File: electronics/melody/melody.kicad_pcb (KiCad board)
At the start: 2 copper layers, 8 parts, among them J1 USB_B, J2 Raspberry_Pi_4, J3 Conn_01x04_Pin, J4 Conn_01x01_Pin, J5 Conn_01x16_Pin, J6 Conn_01x16_Pin, U1 74154, U2 74154

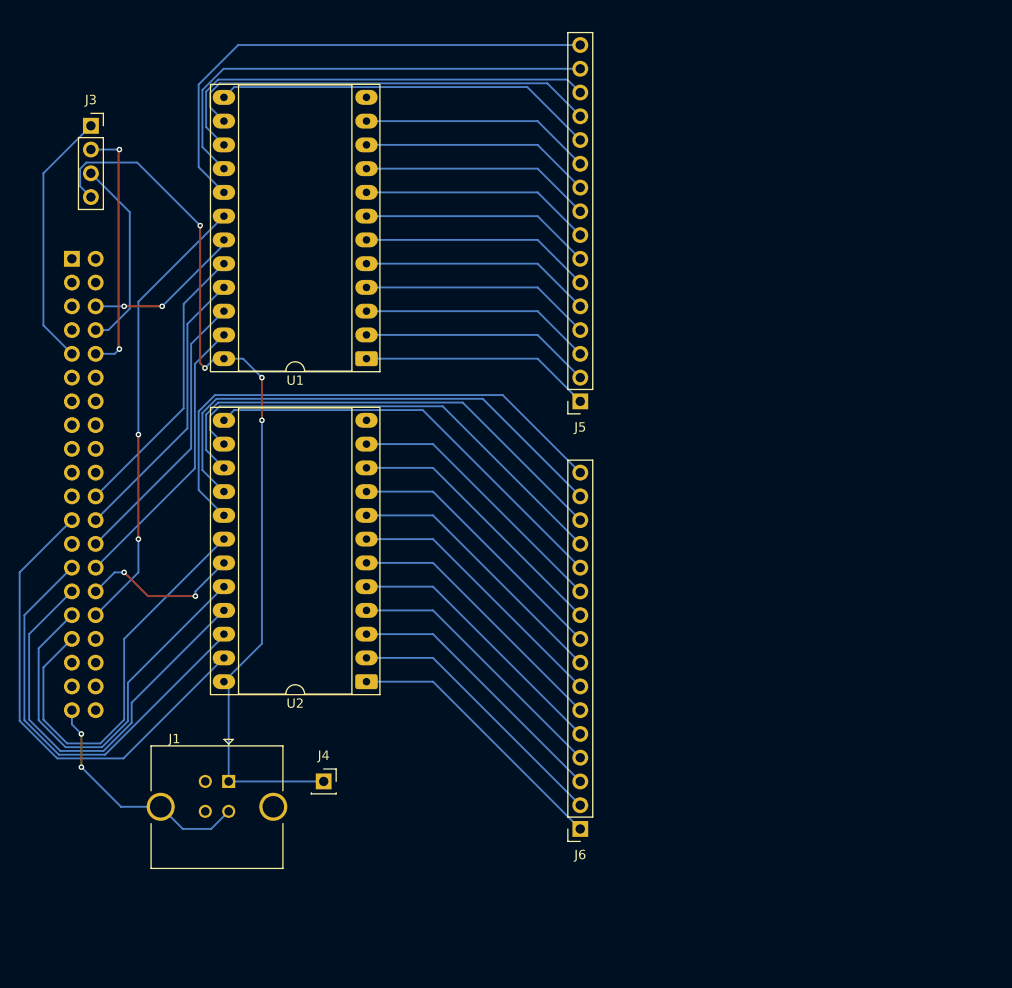
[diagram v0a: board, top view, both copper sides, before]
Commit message: change IC 74->40 + shared power supply for processors + PCB
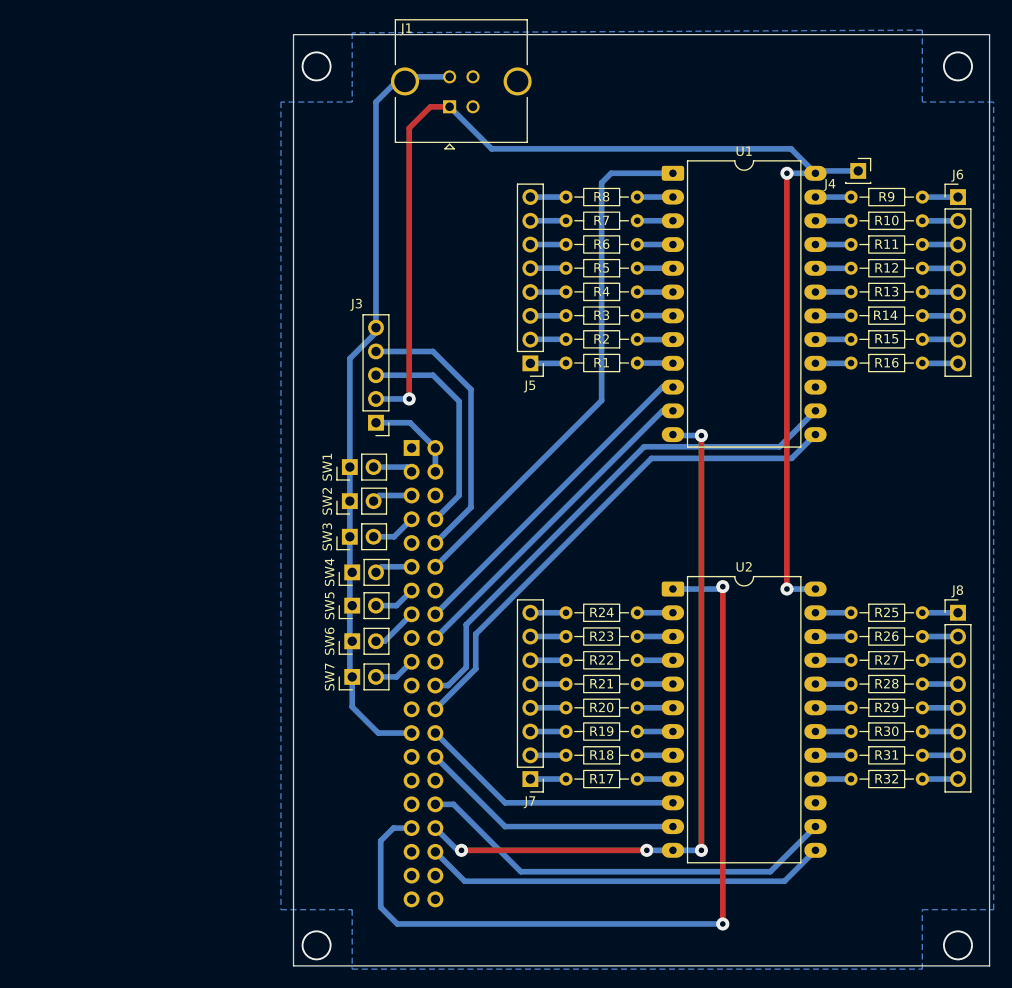
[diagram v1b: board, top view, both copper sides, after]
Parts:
- added J7: Conn_01x08_Pin, Connector_PinHeader_2.54mm:PinHeader_1x08_P2.54mm_Vertical, F.Cu at (135.9, 125.7)
- added J8: Conn_01x08_Pin, Connector_PinHeader_2.54mm:PinHeader_1x08_P2.54mm_Vertical, F.Cu at (181.6, 108.0)
- added R1: 270R, Resistor_THT:R_Axial_DIN0204_L3.6mm_D1.6mm_P7.62mm_Horizontal, F.Cu at (147.3, 81.2)
- added R10: 270R, Resistor_THT:R_Axial_DIN0204_L3.6mm_D1.6mm_P7.62mm_Horizontal, F.Cu at (170.2, 66.0)
- added R11: 270R, Resistor_THT:R_Axial_DIN0204_L3.6mm_D1.6mm_P7.62mm_Horizontal, F.Cu at (170.2, 68.6)
- added R12: 270R, Resistor_THT:R_Axial_DIN0204_L3.6mm_D1.6mm_P7.62mm_Horizontal, F.Cu at (170.2, 71.1)
- added R13: 270R, Resistor_THT:R_Axial_DIN0204_L3.6mm_D1.6mm_P7.62mm_Horizontal, F.Cu at (170.2, 73.6)
- added R14: 270R, Resistor_THT:R_Axial_DIN0204_L3.6mm_D1.6mm_P7.62mm_Horizontal, F.Cu at (170.2, 76.2)
- added R15: 270R, Resistor_THT:R_Axial_DIN0204_L3.6mm_D1.6mm_P7.62mm_Horizontal, F.Cu at (170.2, 78.7)
- added R16: 270R, Resistor_THT:R_Axial_DIN0204_L3.6mm_D1.6mm_P7.62mm_Horizontal, F.Cu at (170.2, 81.3)
- added R17: 330R, Resistor_THT:R_Axial_DIN0204_L3.6mm_D1.6mm_P7.62mm_Horizontal, F.Cu at (147.3, 125.7)
- added R18: 330R, Resistor_THT:R_Axial_DIN0204_L3.6mm_D1.6mm_P7.62mm_Horizontal, F.Cu at (147.3, 123.2)
- added R19: 330R, Resistor_THT:R_Axial_DIN0204_L3.6mm_D1.6mm_P7.62mm_Horizontal, F.Cu at (147.3, 120.7)
- added R2: 270R, Resistor_THT:R_Axial_DIN0204_L3.6mm_D1.6mm_P7.62mm_Horizontal, F.Cu at (147.3, 78.7)
- added R20: 330R, Resistor_THT:R_Axial_DIN0204_L3.6mm_D1.6mm_P7.62mm_Horizontal, F.Cu at (147.3, 118.1)
- added R21: 330R, Resistor_THT:R_Axial_DIN0204_L3.6mm_D1.6mm_P7.62mm_Horizontal, F.Cu at (147.3, 115.6)
- added R22: 330R, Resistor_THT:R_Axial_DIN0204_L3.6mm_D1.6mm_P7.62mm_Horizontal, F.Cu at (147.3, 113.0)
- added R23: 330R, Resistor_THT:R_Axial_DIN0204_L3.6mm_D1.6mm_P7.62mm_Horizontal, F.Cu at (147.3, 110.5)
- added R24: 330R, Resistor_THT:R_Axial_DIN0204_L3.6mm_D1.6mm_P7.62mm_Horizontal, F.Cu at (147.3, 108.0)
- added R25: 330R, Resistor_THT:R_Axial_DIN0204_L3.6mm_D1.6mm_P7.62mm_Horizontal, F.Cu at (170.2, 108.0)
- added R26: 330R, Resistor_THT:R_Axial_DIN0204_L3.6mm_D1.6mm_P7.62mm_Horizontal, F.Cu at (170.2, 110.5)
- added R27: 330R, Resistor_THT:R_Axial_DIN0204_L3.6mm_D1.6mm_P7.62mm_Horizontal, F.Cu at (170.2, 113.0)
- added R28: 330R, Resistor_THT:R_Axial_DIN0204_L3.6mm_D1.6mm_P7.62mm_Horizontal, F.Cu at (170.2, 115.6)
- added R29: 330R, Resistor_THT:R_Axial_DIN0204_L3.6mm_D1.6mm_P7.62mm_Horizontal, F.Cu at (170.2, 118.1)
- added R3: 270R, Resistor_THT:R_Axial_DIN0204_L3.6mm_D1.6mm_P7.62mm_Horizontal, F.Cu at (147.3, 76.2)
- added R30: 330R, Resistor_THT:R_Axial_DIN0204_L3.6mm_D1.6mm_P7.62mm_Horizontal, F.Cu at (170.2, 120.7)
- added R31: 330R, Resistor_THT:R_Axial_DIN0204_L3.6mm_D1.6mm_P7.62mm_Horizontal, F.Cu at (170.2, 123.2)
- added R32: 330R, Resistor_THT:R_Axial_DIN0204_L3.6mm_D1.6mm_P7.62mm_Horizontal, F.Cu at (170.2, 125.7)
- added R4: 270R, Resistor_THT:R_Axial_DIN0204_L3.6mm_D1.6mm_P7.62mm_Horizontal, F.Cu at (147.3, 73.6)
- added R5: 270R, Resistor_THT:R_Axial_DIN0204_L3.6mm_D1.6mm_P7.62mm_Horizontal, F.Cu at (147.3, 71.1)
- added R6: 270R, Resistor_THT:R_Axial_DIN0204_L3.6mm_D1.6mm_P7.62mm_Horizontal, F.Cu at (147.3, 68.6)
- added R7: 270R, Resistor_THT:R_Axial_DIN0204_L3.6mm_D1.6mm_P7.62mm_Horizontal, F.Cu at (147.3, 66.0)
- added R8: 270R, Resistor_THT:R_Axial_DIN0204_L3.6mm_D1.6mm_P7.62mm_Horizontal, F.Cu at (147.3, 63.5)
- added R9: 270R, Resistor_THT:R_Axial_DIN0204_L3.6mm_D1.6mm_P7.62mm_Horizontal, F.Cu at (170.2, 63.5)
- added SW1: SW_Push, Connector_PinHeader_2.54mm:PinHeader_1x02_P2.54mm_Vertical, F.Cu at (116.6, 92.4)
- added SW2: SW_Push, Connector_PinHeader_2.54mm:PinHeader_1x02_P2.54mm_Vertical, F.Cu at (116.6, 96.0)
- added SW3: SW_Push, Connector_PinHeader_2.54mm:PinHeader_1x02_P2.54mm_Vertical, F.Cu at (116.6, 99.8)
- added SW4: SW_Push, Connector_PinHeader_2.54mm:PinHeader_1x02_P2.54mm_Vertical, F.Cu at (116.8, 103.6)
- added SW5: SW_Push, Connector_PinHeader_2.54mm:PinHeader_1x02_P2.54mm_Vertical, F.Cu at (116.8, 107.2)
- added SW6: SW_Push, Connector_PinHeader_2.54mm:PinHeader_1x02_P2.54mm_Vertical, F.Cu at (116.8, 111.0)
- added SW7: SW_Push, Connector_PinHeader_2.54mm:PinHeader_1x02_P2.54mm_Vertical, F.Cu at (116.8, 114.8)
- J3: value Conn_01x04_Pin -> Conn_01x05_Pin; footprint Connector_PinSocket_2.54mm:PinSocket_1x04_P2.54mm_Vertical -> Connector_PinHeader_2.54mm:PinHeader_1x05_P2.54mm_Vertical
- J5, J6: value Conn_01x16_Pin -> Conn_01x08_Pin; footprint Connector_PinSocket_2.54mm:PinSocket_1x16_P2.54mm_Vertical -> Connector_PinHeader_2.54mm:PinHeader_1x08_P2.54mm_Vertical
- U1, U2: value 74154 -> CD4067; footprint Package_DIP:DIP-24_W15.24mm_Socket_LongPads -> Package_DIP:DIP-24_W15.24mm_LongPads
- moved J4 86.8 mm to (170.9, 60.7)
- moved J6 78.7 mm to (181.6, 63.5), turned to 0 degrees
- moved J1 75.9 mm to (127.3, 53.8), turned to 180 degrees
- moved J3 44.0 mm to (119.4, 87.6), turned to 180 degrees
- moved J2 41.6 mm to (123.2, 90.3)
- moved U1 38.3 mm to (151.1, 61.0), turned to 0 degrees
- moved U2 34.2 mm to (151.1, 105.4), turned to 0 degrees
- moved J5 6.71 mm to (135.9, 81.3)
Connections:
- J2 pad 11: unconnected-(J2-GPIO17/SPI1_~{CE1}-Pad11) -> /BT_4
- J2 pad 12: unconnected-(J2-GPIO18/SPI1_~{CE0}/PCM_CLK/PWM0-Pad12) -> /PWM_GREEN
- J2 pad 13: unconnected-(J2-GPIO27/SDIO_DAT3-Pad13) -> /BT_5
- J2 pad 15: unconnected-(J2-GPIO22/SDIO_CLK-Pad15) -> /BT_6
- J2 pad 16: unconnected-(J2-GPIO23/SDIO_CMD-Pad16) -> /G0
- J2 pad 18: unconnected-(J2-GPIO24/SDIO_DAT0-Pad18) -> /G1
- J2 pad 19: unconnected-(J2-MOSI_SPI0/GPIO10-Pad19) -> /BT_7
- J2 pad 2: unconnected-(J2-5V-Pad2)_1 -> /5V_CPU
- J2 pad 22: /G3 -> /G2
- J2 pad 23: /R0 -> unconnected-(J2-SCLK_SPI0/GPIO11-Pad23)
- J2 pad 24: /G2 -> /G3
- J2 pad 26: /G1 -> /R0
- J2 pad 27: /R1 -> unconnected-(J2-ID_SD_I2C0/GPIO00-Pad27)
- J2 pad 28: /G0 -> /R1
- J2 pad 29: /R2 -> unconnected-(J2-GPCLK1/GPIO05-Pad29)
- J2 pad 3: unconnected-(J2-SDA_I2C1/GPIO02-Pad3) -> /BT_1
- J2 pad 31: /R3 -> unconnected-(J2-GPCLK2/GPIO06-Pad31)
- J2 pad 32: /PWM_GREEN -> /R2
- J2 pad 36: unconnected-(J2-GPIO16/SPI1_~{CE2}-Pad36) -> /R3
- J2 pad 4: unconnected-(J2-5V-Pad2) -> /5V_CPU
- J2 pad 5: unconnected-(J2-SCL_I2C1/GPIO03-Pad5) -> /BT_2
- J2 pad 7: unconnected-(J2-GPCLK0/GPIO04-Pad7) -> /BT_3
- J3 pad 1: GND -> /5V_CPU
- J3 pad 2: /MELODY_RX -> /5V_OTHERS
- J3 pad 4: /5V_OTHERS -> /MELODY_RX
- J6 pad 1: /RED_01 -> /GREEN_09
- J6 pad 2: /RED_02 -> /GREEN_10
- J6 pad 3: /RED_03 -> /GREEN_11
- J6 pad 4: /RED_04 -> /GREEN_12
- J6 pad 5: /RED_05 -> /GREEN_13
- J6 pad 6: /RED_06 -> /GREEN_14
- J6 pad 7: /RED_07 -> /GREEN_15
- J6 pad 8: /RED_08 -> /GREEN_16
- U1 pad 1: /GREEN_01 -> /PWM_GREEN
- U1 pad 10: /GREEN_10 -> /G0
- U1 pad 11: /GREEN_11 -> /G1
- U1 pad 13: /GREEN_12 -> /G3
- U1 pad 14: /GREEN_13 -> /G2
- U1 pad 15: /GREEN_14 -> GND
- U1 pad 16: /GREEN_15 -> Net-(U1-I15)
- U1 pad 17: /GREEN_16 -> Net-(U1-I14)
- U1 pad 18: /PWM_GREEN -> Net-(U1-I13)
- U1 pad 19: GND -> Net-(U1-I12)
- U1 pad 2: /GREEN_02 -> Net-(U1-I7)
- U1 pad 20: /G3 -> Net-(U1-I11)
- U1 pad 21: /G2 -> Net-(U1-I10)
- U1 pad 22: /G1 -> Net-(U1-I9)
- U1 pad 23: /G0 -> Net-(U1-I8)
- U1 pad 3: /GREEN_03 -> Net-(U1-I6)
- U1 pad 4: /GREEN_04 -> Net-(U1-I5)
- U1 pad 5: /GREEN_05 -> Net-(U1-I4)
- U1 pad 6: /GREEN_06 -> Net-(U1-I3)
- U1 pad 7: /GREEN_07 -> Net-(U1-I2)
- U1 pad 8: /GREEN_08 -> Net-(U1-I1)
- U1 pad 9: /GREEN_09 -> Net-(U1-I0)
- U2 pad 1: /RED_01 -> /PWM_RED
- U2 pad 10: /RED_10 -> /R0
- U2 pad 11: /RED_11 -> /R1
- U2 pad 13: /RED_12 -> /R3
- U2 pad 14: /RED_13 -> /R2
- U2 pad 15: /RED_14 -> GND
- U2 pad 16: /RED_15 -> Net-(U2-I15)
- U2 pad 17: /RED_16 -> Net-(U2-I14)
- U2 pad 18: /PWM_RED -> Net-(U2-I13)
- U2 pad 19: GND -> Net-(U2-I12)
- U2 pad 2: /RED_02 -> Net-(U2-I7)
- U2 pad 20: /R3 -> Net-(U2-I11)
- U2 pad 21: /R2 -> Net-(U2-I10)
- U2 pad 22: /R1 -> Net-(U2-I9)
- U2 pad 23: /R0 -> Net-(U2-I8)
- U2 pad 3: /RED_03 -> Net-(U2-I6)
- U2 pad 4: /RED_04 -> Net-(U2-I5)
- U2 pad 5: /RED_05 -> Net-(U2-I4)
- U2 pad 6: /RED_06 -> Net-(U2-I3)
- U2 pad 7: /RED_07 -> Net-(U2-I2)
- U2 pad 8: /RED_08 -> Net-(U2-I1)
- U2 pad 9: /RED_09 -> Net-(U2-I0)
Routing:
- net GND: track 88.3 -> 159.3 mm, vias 6 -> 4
- net /RED_16: track 57.2 -> 3.81 mm
- net /GREEN_16: track 55.2 -> 3.82 mm
- net /RED_15: track 54.7 -> 3.81 mm
- net /RED_14: track 52.2 -> 3.81 mm
- net /GREEN_15: track 50.7 -> 3.82 mm
- net /RED_13: track 49.7 -> 3.81 mm
- net /PWM_RED: track 44.4 -> 89.8 mm, vias 0 -> 2
- net /GREEN_14: track 47.6 -> 3.82 mm
- net /RED_12: track 45.5 -> 3.81 mm
- net /GREEN_13: track 45.1 -> 3.82 mm
- net /5V_OTHERS: track 97.9 -> 135.1 mm, vias 4 -> 3
- net /GREEN_12: track 40.9 -> 3.82 mm
- net /RED_11: track 29.4 -> 3.81 mm
- net /RED_09: track 29.4 -> 3.81 mm
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- added copper zone on B.Cu, net GND
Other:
- board outline added: 74.4 x 99.6 mm
